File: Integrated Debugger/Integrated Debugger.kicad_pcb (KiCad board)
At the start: 4 copper layers, 36.8 x 16.4 mm, 60 parts, among them J1 B2B GT-B0353FSV06-08B0201, J2 USB_C (PC <-> Host), J3 FPC socket 10P, J4 20021521-00010T1LF, J5 PWR, Q1 NMOS DMN2991UDA-7B, SW1 RESET, SW2 BOOT, SW3 Solar Override, SW4 Target Override, U1 TPS7A2633DRVR, U2 USBULC6-2M6, U3 STM32F103CBUx, U4 TXB0106RGY, U5 TPS22914, U8 TPS22914, Y1 8MHz

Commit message: PCB improvements
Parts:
- removed D7: PMEG3005EL,315, Picoballoon Passives:Diode SOD-882
- removed TP1: tTDI, Picoballoon Mechanical & Misc:TestPoint
- moved C12 0.68 mm to (152.6, 90.9), turned to 0 degrees
- renumbered C3 to C1, C1 to C10, C12 to C11, C14 to C12, C16 to C13, C2 to C14, C10 to C15, C11 to C16, C4 to C2, C5 to C3, C6 to C4, C7 to C5, C8 to C6, C9 to C7, C13 to C8, C15 to C9, D2 to D1, D3 to D2, D4 to D3, D5 to D4, D6 to D5, R10 to R1, R14 to R10, R15 to R11, R16 to R12, R1 to R13, R20 to R14, R4 to R15, R5 to R16, R6 to R17, R7 to R18, R9 to R2, R8 to R3, R2 to R4, R3 to R5, R11 to R6, R12 to R7, R19 to R8, R13 to R9, SW2 to SW1, SW1 to SW2, U2 to U1, U3 to U2, U4 to U3, U1 to U4, U8 to U5, U5 to U6
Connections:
- net /Target Frontend/xRST renamed /Target/xRST
- net /Target Frontend/xRXD renamed Net-(RN1H-R8.2)
- net /Target Frontend/xTCK renamed Net-(RN1D-R4.2)
- net /Target Frontend/xTDI renamed Net-(RN1B-R2.2)
- net /Target Frontend/xTDO renamed Net-(RN1E-R5.2)
- net /Target Frontend/xTMS renamed Net-(RN1C-R3.2)
- net /Target Frontend/xTXD renamed Net-(RN1F-R6.2)
- J4 pad 2: GND -> /Target/tTDI
- RN1 pad 2: Net-(RN1B-R2.1) -> /Target/tTDI
- U2 pad 11: /MCU/i.TMS_DIR -> unconnected-(U2-PA1-Pad11)
- U6 pad A1: /Power/V_TARGET_UNFILT -> V_TARGET
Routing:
- net Net-(RN1B-R2.1): track 4.02 -> 0.00 mm, vias 1 -> 0
- net /Target/tTDI: track 0.00 -> 2.86 mm
- net V_TARGET: track 54.8 -> 52.5 mm
- net /Power/V_TARGET_UNFILT: track 1.70 -> 0.00 mm
- net V_SOLAR: track 15.1 -> 13.7 mm
- net /MCU/i.RX: track 18.8 -> 17.9 mm
- net /Target/tRXD: track 19.9 -> 19.1 mm
- net /MCU/i.RST_SEN: track 18.8 -> 18.3 mm
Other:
- board text added: "SOLAR POWER"
- board text added: "TARGET POWER"
- board text removed: "SOLAR POWER MANUAL CONTROL"
- board text removed: "TARGET POWER MANUAL CONTROL"
- board text removed: "TDI"

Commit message: PCB improvements
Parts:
- moved R14 0.08 mm to (155.4, 88.9)
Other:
- board text added: "ENIG"
- board text added: "JLC04081H-3313 JLCPCB stackup"
- board text removed: "HAL SnPb"
- board text removed: "JLC04081H-3313 JLCPCB Stackup"

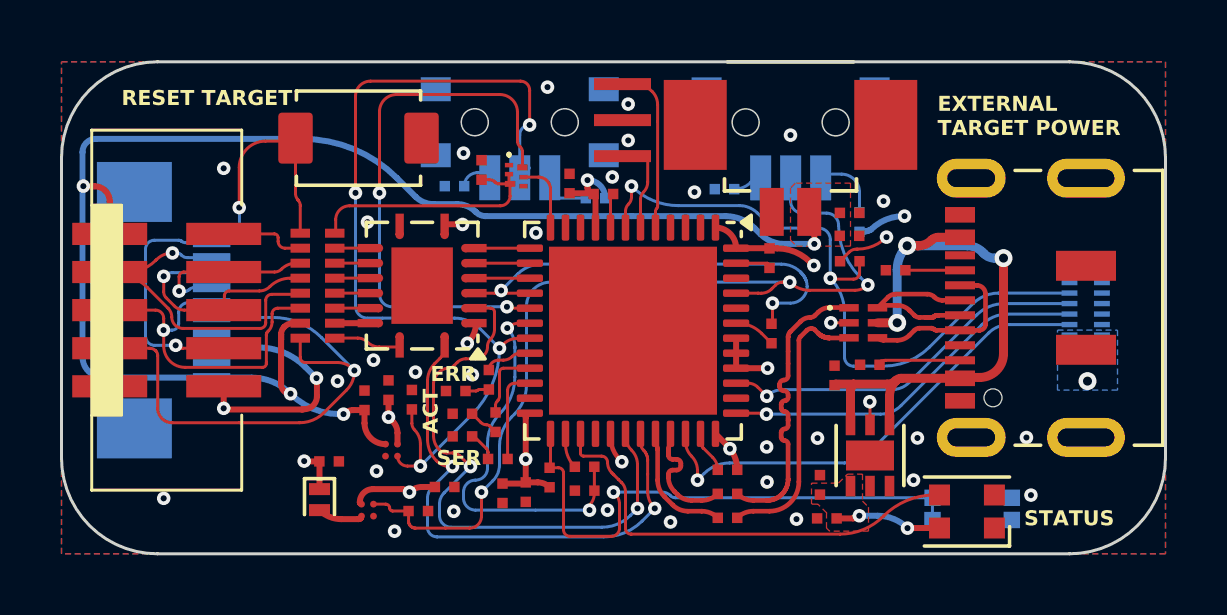
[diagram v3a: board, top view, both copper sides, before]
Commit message: feat: debugger flip swd connector, usb patch + stackup change
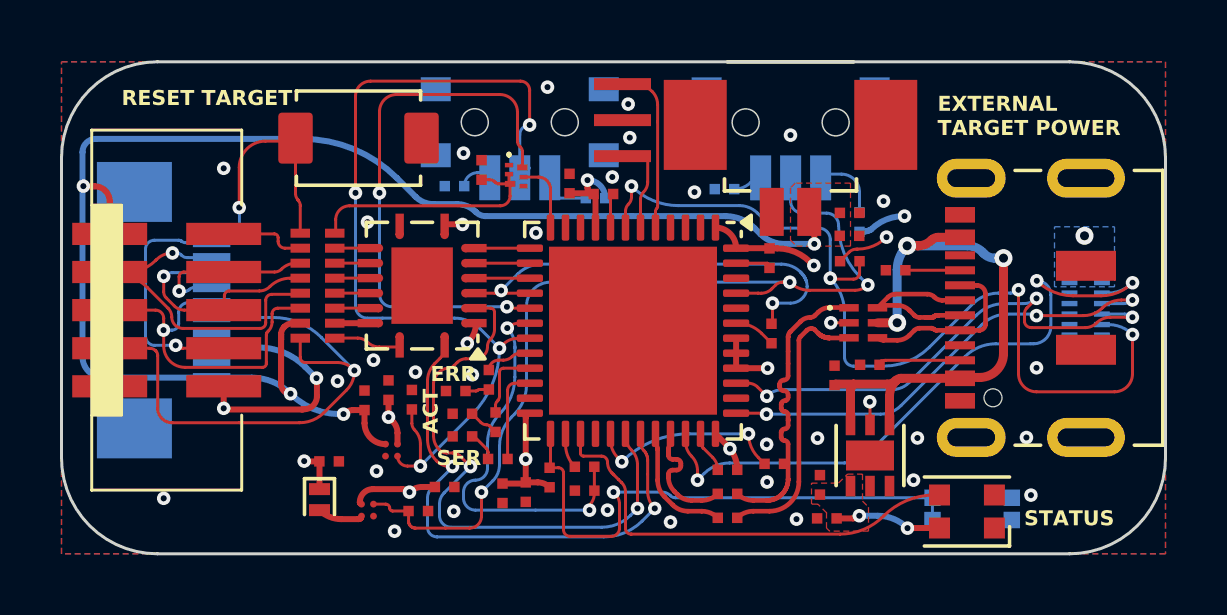
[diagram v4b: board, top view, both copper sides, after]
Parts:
- added R19: 1.5kΩ, Picoballoon Passives:Resistor 0201, F.Cu at (167.5, 91.0)
- turned J1 to -90 degrees
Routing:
- net /MCU/~{RST}: track 22.7 -> 30.6 mm, vias 2 -> 4
- net /MCU/USB.PD: track 0.95 -> 6.76 mm, vias 1 -> 2
- net /MCU/SWD.IO: track 16.0 -> 21.7 mm, vias 1 -> 3
- net /MCU/TRACESWO: track 12.4 -> 17.1 mm, vias 1 -> 3
- net /MCU/SWD.CLK: track 12.3 -> 15.8 mm, vias 1 -> 3
- net GND: vias 32 -> 33
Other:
- board text added: "0.01524 mm"
- board text added: "0.7 mm"
- board text added: "1.0297 mm"
- board text added: "3.8"
- board text added: "4.4"
- board text added: "JLC04101H-3313 JLCPCB stackup"
- board text removed: "0.01 mm"
- board text removed: "0.5 mm"
- board text removed: "0.8192 mm"
- board text removed: "3.3"
- board text removed: "4.5"
- board text removed: "JLC04081H-3313 JLCPCB stackup"
- board text removed: "SWD"

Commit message: Improve routing, placement & decorations, final check pass
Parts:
- removed G***: LOGO, LOGO
- moved R17 0.63 mm to (160.9, 81.8), turned to -90 degrees
- moved R8 0.51 mm to (167.3, 86.2)
- moved SW2 0.40 mm to (153.6, 79.7)
- moved SW3 0.22 mm to (168.0, 79.4)
- moved SW4 0.22 mm to (159.0, 79.4)
- moved R18 0.12 mm to (156.7, 81.7)
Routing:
- net +3.3V: track 26.4 -> 20.2 mm
- net GND: track 7.73 -> 2.91 mm, vias 33 -> 56
- net /Target/tRST: track 17.9 -> 15.2 mm
- net V_TARGET: track 52.5 -> 50.4 mm
- net /MCU/i.TDO: track 15.2 -> 13.4 mm
- net Net-(SW1-B): track 18.4 -> 17.0 mm
- net /MCU/SOL_EN: track 30.8 -> 30.0 mm
- net /MCU/TARGET_EN: track 30.6 -> 29.9 mm
- net Net-(R18-Pad1): track 1.16 -> 1.69 mm
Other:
- board text added: "BOOT"
- board text added: "EXTERNAL POWER"
- board text added: "Integrated Debugger"
- board text added: "RESET"
- board text added: "SN_NUMBER"
- board text added: "V1.0"
- board text removed: "EXTERNAL TARGET POWER"
- board text removed: "Picoballoon Integrated Debugger"
- board text removed: "RESET TARGET"
- board text removed: "V0.1"
